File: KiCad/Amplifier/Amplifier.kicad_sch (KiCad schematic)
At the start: 91 parts, among them Q10 BD140, Q7 BD139, Q8 BD139, Q9 BD140, U1 AD8021AR, U2 AD8017ARZ

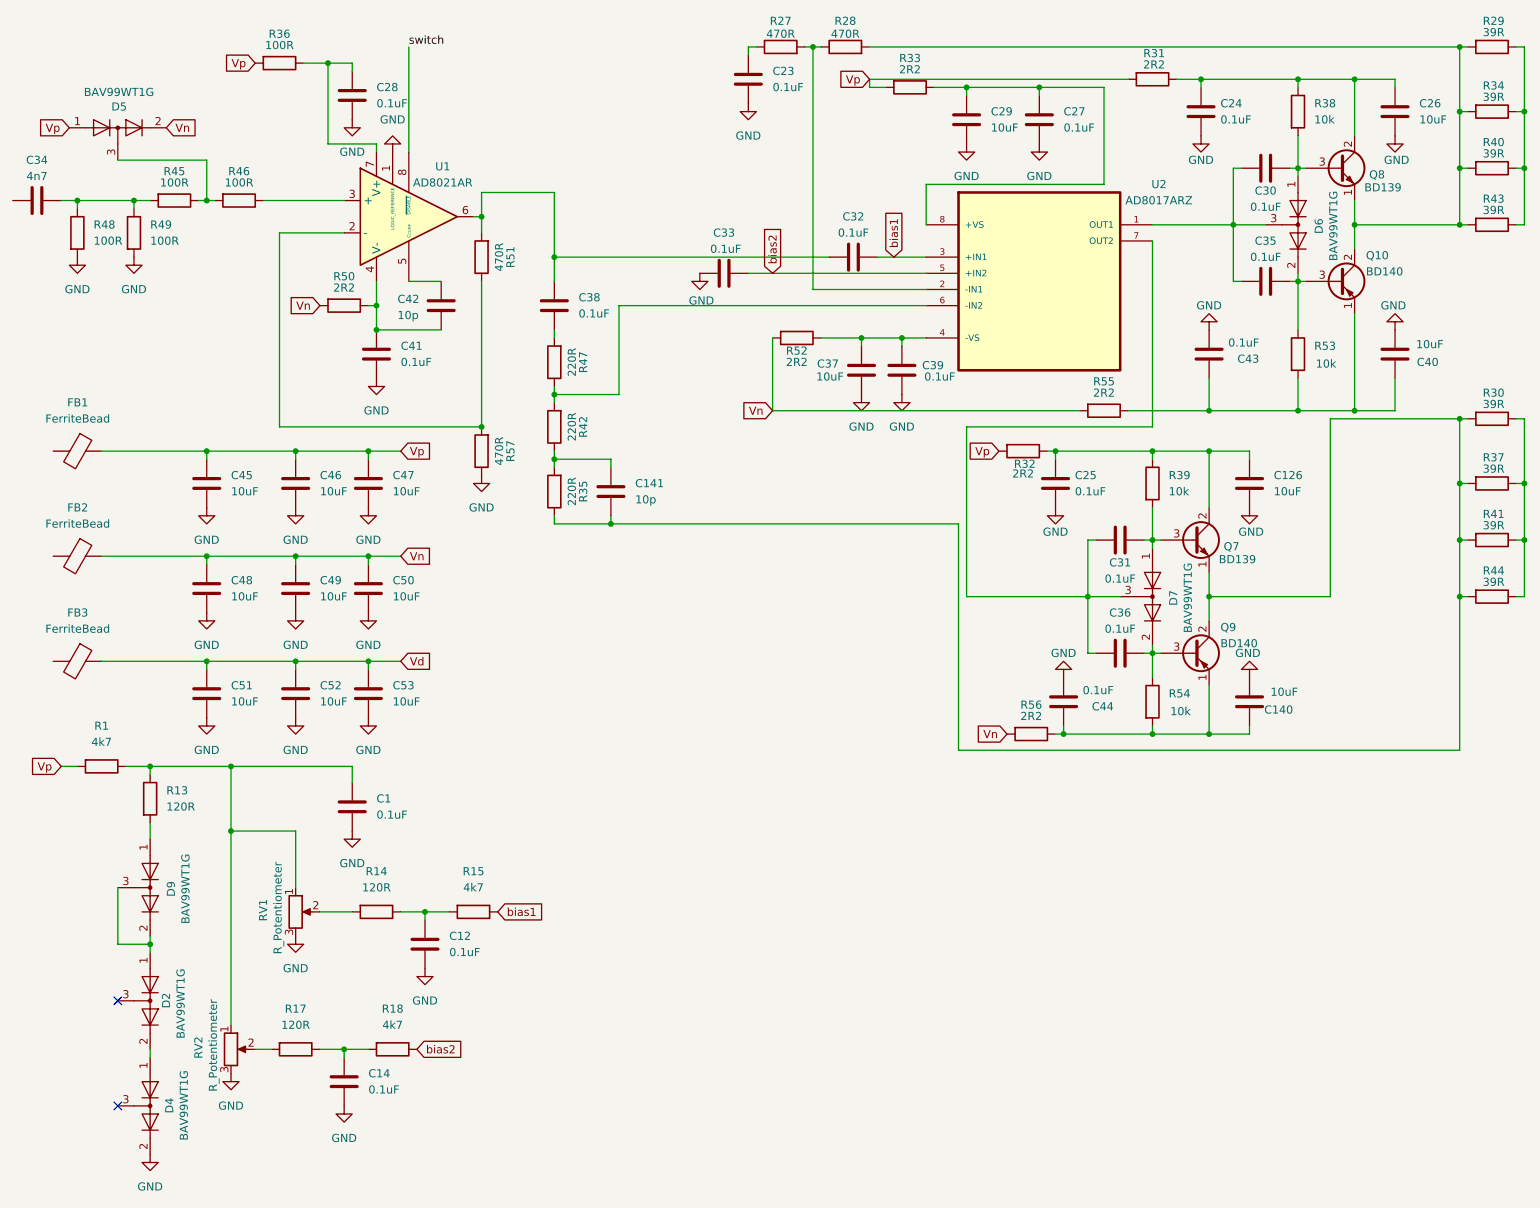
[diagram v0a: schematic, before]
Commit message: update Ampilfier
Schematic updated with separate pages.
all footprints added.
to do :
HF Part
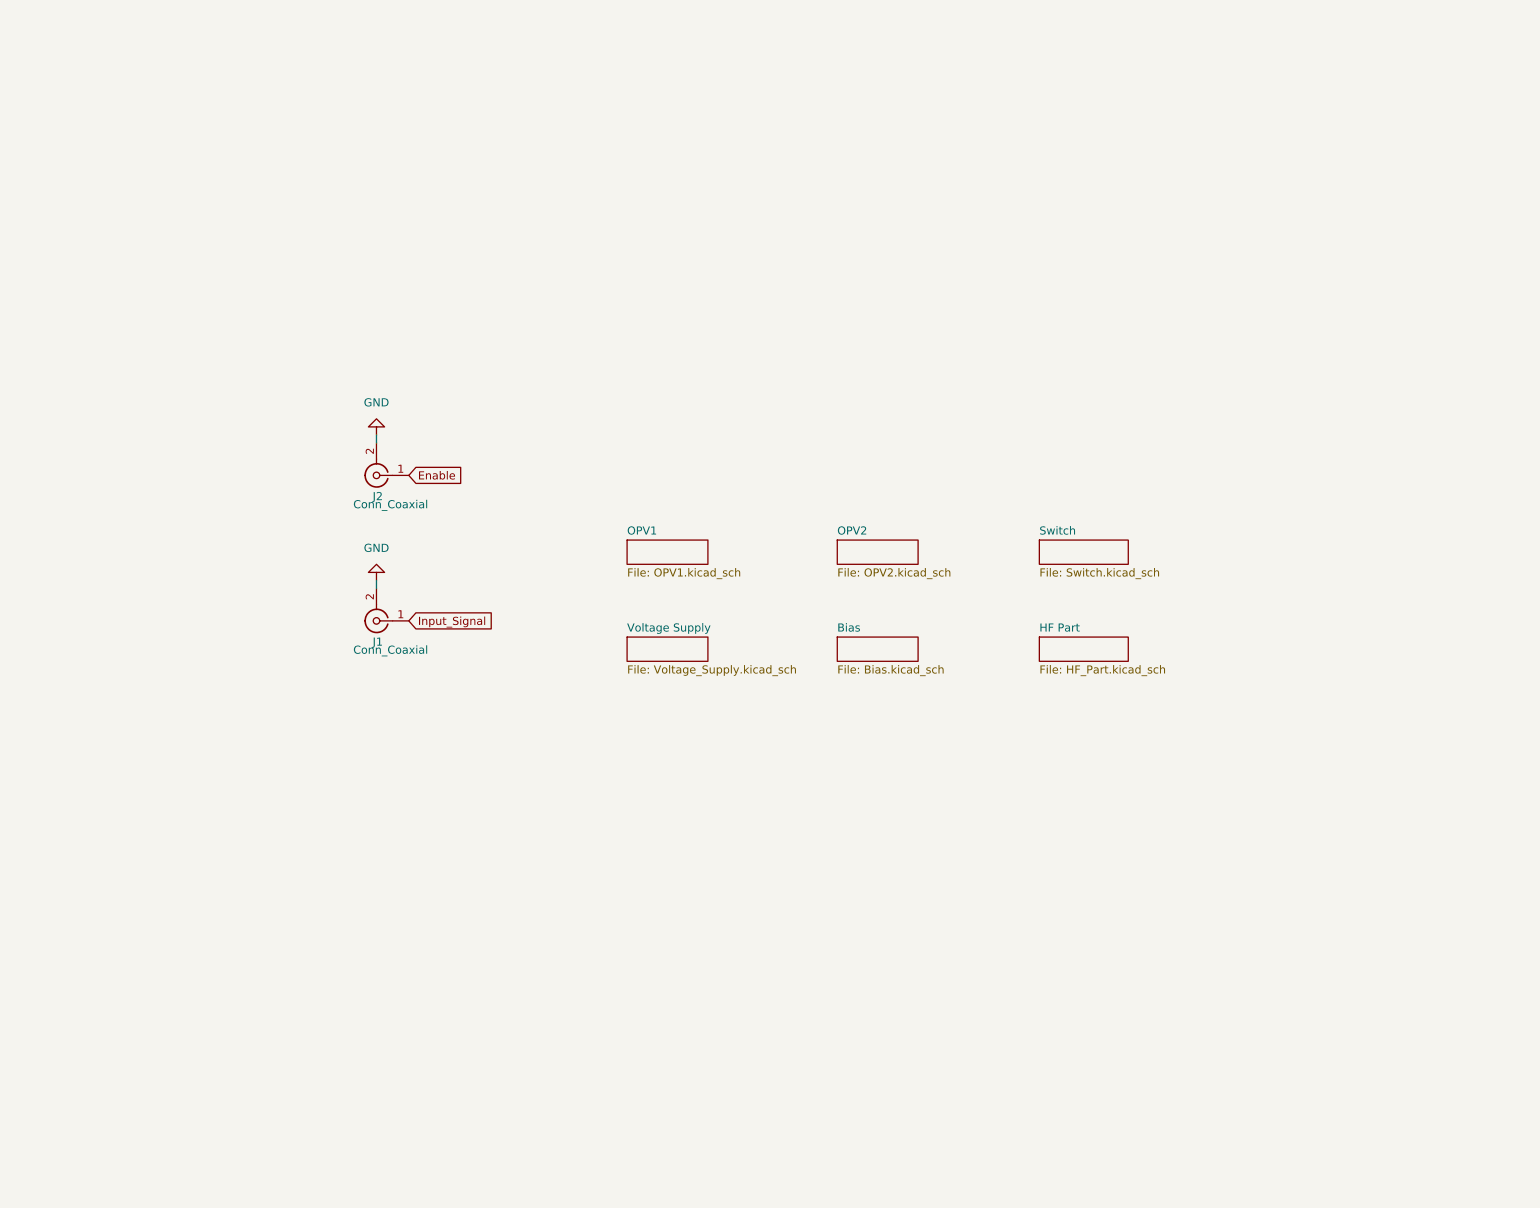
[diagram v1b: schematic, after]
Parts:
- removed C1, C12, C14, C23, C24, C25, C27, C28, C30, C31, C32, C33, C35, C36, C38, C39, C41, C43, C44: 0.1uF, Capacitor_SMD:C_0603_1608Metric_Pad1.08x0.95mm_HandSolder, symbol Device:C
- removed C126, C140, C26, C29, C37, C40, C45, C46, C47, C48, C49, C50, C51, C52, C53: 10uF, Capacitor_SMD:C_0603_1608Metric_Pad1.08x0.95mm_HandSolder, symbol Device:C
- removed C141, C42: 10p, Capacitor_SMD:C_0603_1608Metric_Pad1.08x0.95mm_HandSolder, symbol Device:C
- removed C34: 4n7, Capacitor_SMD:C_0603_1608Metric_Pad1.08x0.95mm_HandSolder, symbol Device:C
- removed D2, D4, D5, D6, D7, D9: BAV99WT1G, Package_TO_SOT_SMD:SOT-323_SC-70, symbol Diode:BAV99
- removed FB1, FB2, FB3: FerriteBead, Library:BLM21PG300SN1B, symbol Device:FerriteBead
- removed Q10, Q9: BD140, Package_TO_SOT_THT:TO-126-3_Vertical, symbol Transistor_BJT:BD140
- removed Q7, Q8: BD139, Package_TO_SOT_THT:TO-126-3_Vertical, symbol Transistor_BJT:BD139
- removed R1, R15, R18: 4k7, Resistor_SMD:R_0603_1608Metric_Pad0.98x0.95mm_HandSolder, symbol Device:R
- removed R13, R14, R17: 120R, Resistor_SMD:R_0603_1608Metric_Pad0.98x0.95mm_HandSolder, symbol Device:R
- removed R27, R28, R51, R57: 470R, Resistor_SMD:R_0603_1608Metric_Pad0.98x0.95mm_HandSolder, symbol Device:R
- removed R29, R30, R34, R37, R40, R41, R43, R44: 39R, Resistor_SMD:R_0603_1608Metric_Pad0.98x0.95mm_HandSolder, symbol Device:R
- removed R31, R32, R33, R50, R52, R55, R56: 2R2, Resistor_SMD:R_0603_1608Metric_Pad0.98x0.95mm_HandSolder, symbol Device:R
- removed R35, R42, R47: 220R, Resistor_SMD:R_0603_1608Metric_Pad0.98x0.95mm_HandSolder, symbol Device:R
- removed R36, R45, R46, R48, R49: 100R, Resistor_SMD:R_0603_1608Metric_Pad0.98x0.95mm_HandSolder, symbol Device:R
- removed R38, R39, R53, R54: 10k, Resistor_SMD:R_0603_1608Metric_Pad0.98x0.95mm_HandSolder, symbol Device:R
- removed RV1, RV2: R_Potentiometer, symbol Device:R_Potentiometer
- removed U1: AD8021AR, Package_SO:SOIC-8_3.9x4.9mm_P1.27mm, symbol Amplifier_Operational:AD8021AR
- removed U2: AD8017ARZ, Package_SO:SOIC-8_3.9x4.9mm_P1.27mm, symbol New_Library_0:AD8017ARZ
- added J1, J2: Conn_Coaxial, Connector_Coaxial:SMA_Amphenol_901-144_Vertical, symbol Connector:Conn_Coaxial
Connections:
- net GND: now also J1.2 (Ext), J2.2 (Ext)
- new net Enable: J2.1 (In)
- new net Input_Signal: J1.1 (In)
- no-connect marks 2 -> 0
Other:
- added sheet Bias (Bias.kicad_sch)
- added sheet HF Part (HF_Part.kicad_sch)
- added sheet OPV1 (OPV1.kicad_sch)
- added sheet OPV2 (OPV2.kicad_sch)
- added sheet Switch (Switch.kicad_sch)
- added sheet Voltage Supply (Voltage_Supply.kicad_sch)

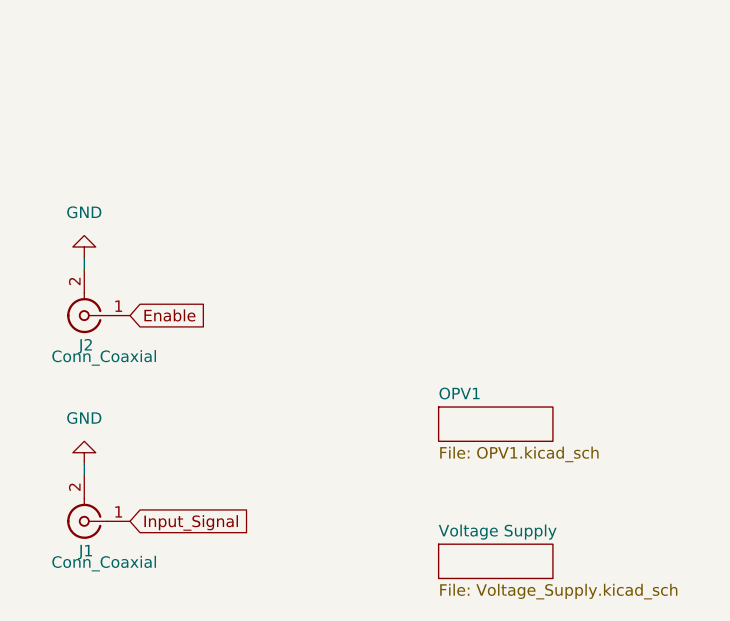
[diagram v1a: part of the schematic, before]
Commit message: Platinenentwurf
die Platine wurde aufgebaut. Kontrolle fehlt
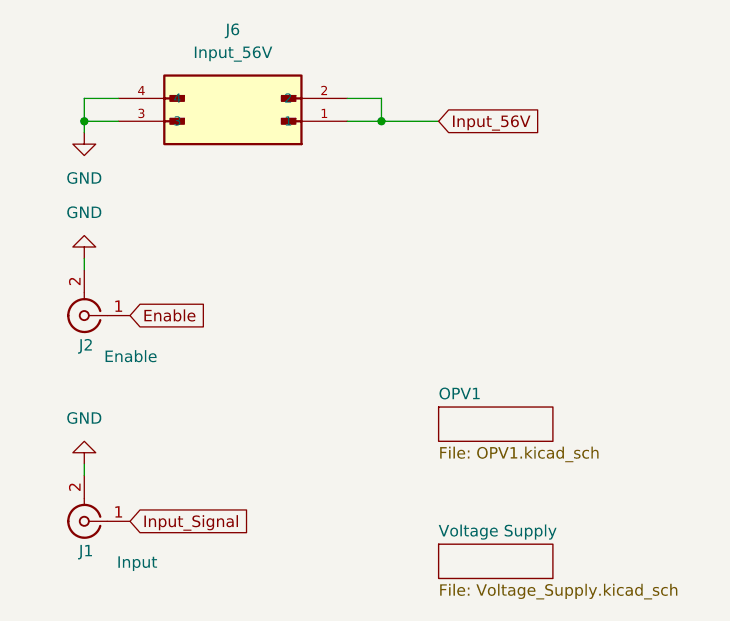
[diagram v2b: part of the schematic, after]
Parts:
- added J6: Input_56V, Library:MOLEX_26013115, symbol New_Library_0:Molex_26013115
- J1: value Conn_Coaxial -> Input
- J2: value Conn_Coaxial -> Enable
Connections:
- net GND: now also J6.3, J6.4
- new net Input_56V: J6.1, J6.2

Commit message: Update PCB
update PCB
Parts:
- removed J6: Input_56V, Library:MOLEX_26013115, symbol New_Library_0:Molex_26013115
- added H1, H2, H3, H4: MountingHole, MountingHole:MountingHole_3.2mm_M3_Pad, symbol Mechanical:MountingHole
- added J6: Input_56V, Library:MOLEX_26013115, symbol Connector_Generic:Conn_02x02_Counter_Clockwise
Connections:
- net GND: now also J6.3 (Pin_3), J6.4 (Pin_4)
- net Input_56V: now also J6.1 (Pin_1), J6.2 (Pin_2)
